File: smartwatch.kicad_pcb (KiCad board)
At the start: 2 copper layers, 34.4 x 215.2 mm, 104 parts, among them J1 505148-0408, J2 505147-0490, J3 505110-2491, J4 503480-0600, Q1 Si1308EDL, Q2 Si1308EDL, Q3 Si1308EDL, SW1 SKTDLDE010, SW2 SKTDLDE010, SW3 SKTDLDE010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

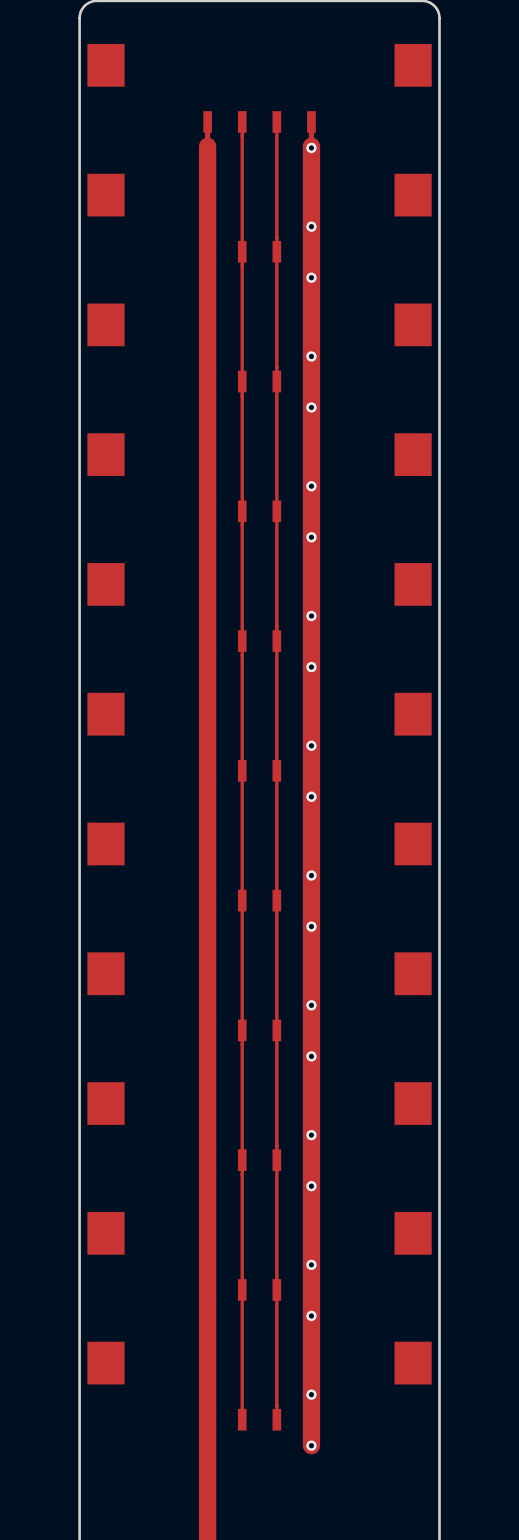
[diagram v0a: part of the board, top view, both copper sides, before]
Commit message: FIX: increase thickness of traces on wristband clasp so the pads extend under the solder resist.
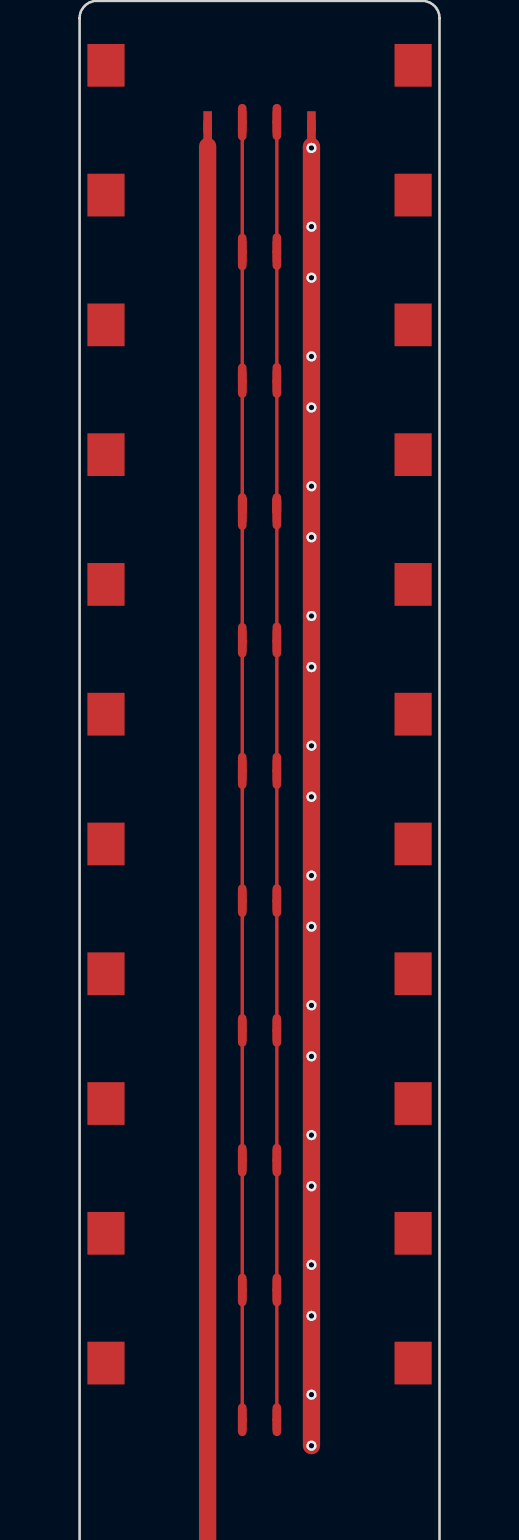
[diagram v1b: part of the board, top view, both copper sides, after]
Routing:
- net Net-(J2-Pad2): track 75.0 -> 77.3 mm
- net Net-(J2-Pad3): track 75.0 -> 77.3 mm
- net -BATT: track 265.9 -> 267.4 mm
